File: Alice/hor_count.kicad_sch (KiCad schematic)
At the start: 270 parts, among them Q1 PASS, Q159 NOT_OC, Q160 NOT_OC, Q161 NOT_OC, Q162 NOT_OC, Q163 NOT_OC, Q164 NOT_OC, Q165 NOT_OC, Q166 NOT_OC, Q167 NOT_OC, Q168 NOT_OC, Q169 NOT_OC, Q170 NOT_OC, Q171 NOT_OC, Q172 NOT_OC, Q173 NOT_OC, Q174 NOT_OC, Q175 NOT_OC, Q176 NOT_OC, Q177 NOT_OC, Q178 NOT_OC, Q179 NOT_OC, Q180 NOT_OC, Q181 NOT_OC, Q182 NOT_OC, Q183 NOT_OC, Q184 NOT_OC, Q185 NOT_OC, Q186 NOT_OC, Q187 NOT_OC, Q188 NOT_OC, Q189 NOT_OC, Q190 NOT_OC, Q191 NOT_OC, Q192 NOT_OC, Q193 NOT_OC, Q194 NOT_OC, Q195 NOT_OC, Q196 NOT_OC, Q197 NOT_OC, Q198 NOT_OC, Q199 NOT_OC, Q2 PASS, Q200 NOT_OC, Q201 NOT_OC, Q202 NOT_OC, Q203 NOT_OC, Q204 NOT_OC, Q205 NOT_OC, Q206 NOT_OC, Q207 NOT_OC, Q208 NOT_OC, Q209 NOT_OC, Q210 NOT_OC, Q211 NOT_OC, Q212 NOT_OC, Q213 NOT_OC, Q214 NOT_OC, Q215 NOT_OC, Q216 NOT_OC, Q217 NOT_OC, Q218 NOT_OC, Q219 NOT_OC, Q220 NOT_OC, Q221 NOT_OC, Q222 NOT_OC, Q223 NOT_OC, Q224 NOT_OC, Q225 NOT_OC, Q226 NOT_OC, Q227 NOT_OC, Q228 NOT_OC, Q229 NOT_OC, Q230 NOT_OC, Q231 NOT_OC, Q232 NOT_OC, Q233 NOT_OC, Q234 NOT_OC, Q235 NOT_OC, Q236 NOT_OC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

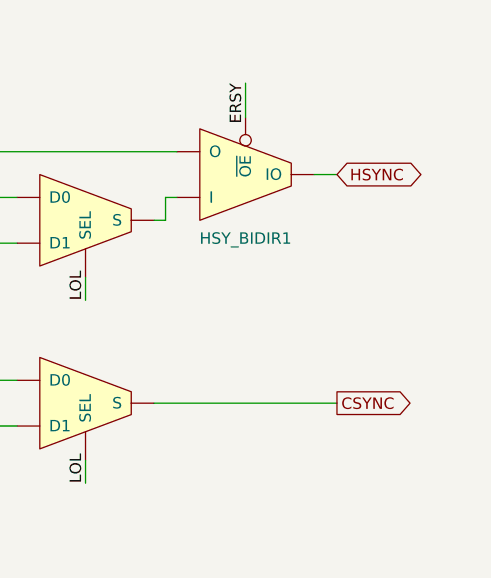
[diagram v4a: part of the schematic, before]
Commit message: RGA bus added (WIP), I/Os renamed with PAD_ prefix
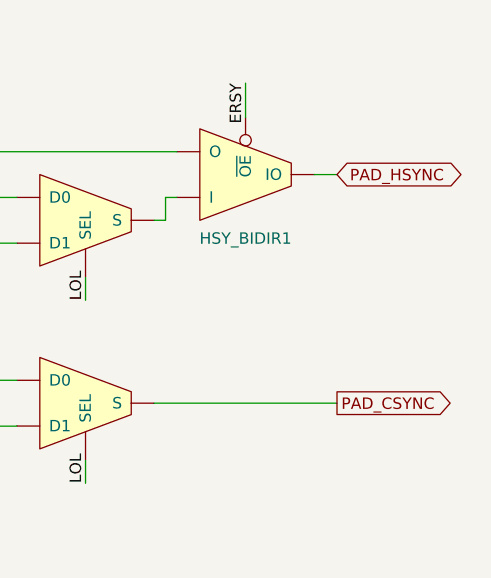
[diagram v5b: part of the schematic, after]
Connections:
- net CSYNC renamed PAD_CSYNC
- net HSYNC renamed PAD_HSYNC
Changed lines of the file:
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@@
     )
   )
-  (global_label "CSYNC" (shape output) (at 464.82 248.92 0) (fields_autoplaced)
+  (global_label "PAD_CSYNC" (shape output) (at 464.82 248.92 0) (fields_autoplaced)
     (effects (font (size 1.27 1.27)) (justify left))
-    (property "Intersheet References" "${INTERSHEET_REFS}" (id 0) (at 473.4017 248.8406 0)
+    (property "Intersheet References" "${INTERSHEET_REFS}" (id 0) (at 477.9979 248.8406 0)
       (effects (font (size 1.27 1.27)) (justify left) hide)
     )
@@
     )
   )
-  (global_label "HSYNC" (shape bidirectional) (at 464.82 223.52 0) (fields_autoplaced)
+  (global_label "PAD_HSYNC" (shape bidirectional) (at 464.82 223.52 0) (fields_autoplaced)
     (effects (font (size 1.27 1.27)) (justify left))
-    (property "Intersheet References" "${INTERSHEET_REFS}" (id 0) (at 473.4621 223.4406 0)
+    (property "Intersheet References" "${INTERSHEET_REFS}" (id 0) (at 478.0583 223.4406 0)
       (effects (font (size 1.27 1.27)) (justify left) hide)
     )

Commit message: Some refactoring : BEAMCON0 and BPLCON0 moved to the top sheet, CLOCKGEN added
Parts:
- removed BEAMCON0_LB0, BEAMCON0_LB10, BEAMCON0_LB11, BEAMCON0_LB2, BEAMCON0_LB3, BEAMCON0_LB4, BEAMCON0_LB8: LB2, symbol NMOS:LB2
- removed NOT_11: NOT, symbol NMOS:NOT
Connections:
- net RESET: now also OR_7.2; no longer OR_7.3
- net RHSH: now also OR_7.3; no longer OR_7.2
- no-connect marks 8 -> 1
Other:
- moved on the sheet: HEND_FF1, HSY_BIDIR1, VARHSY_SR1

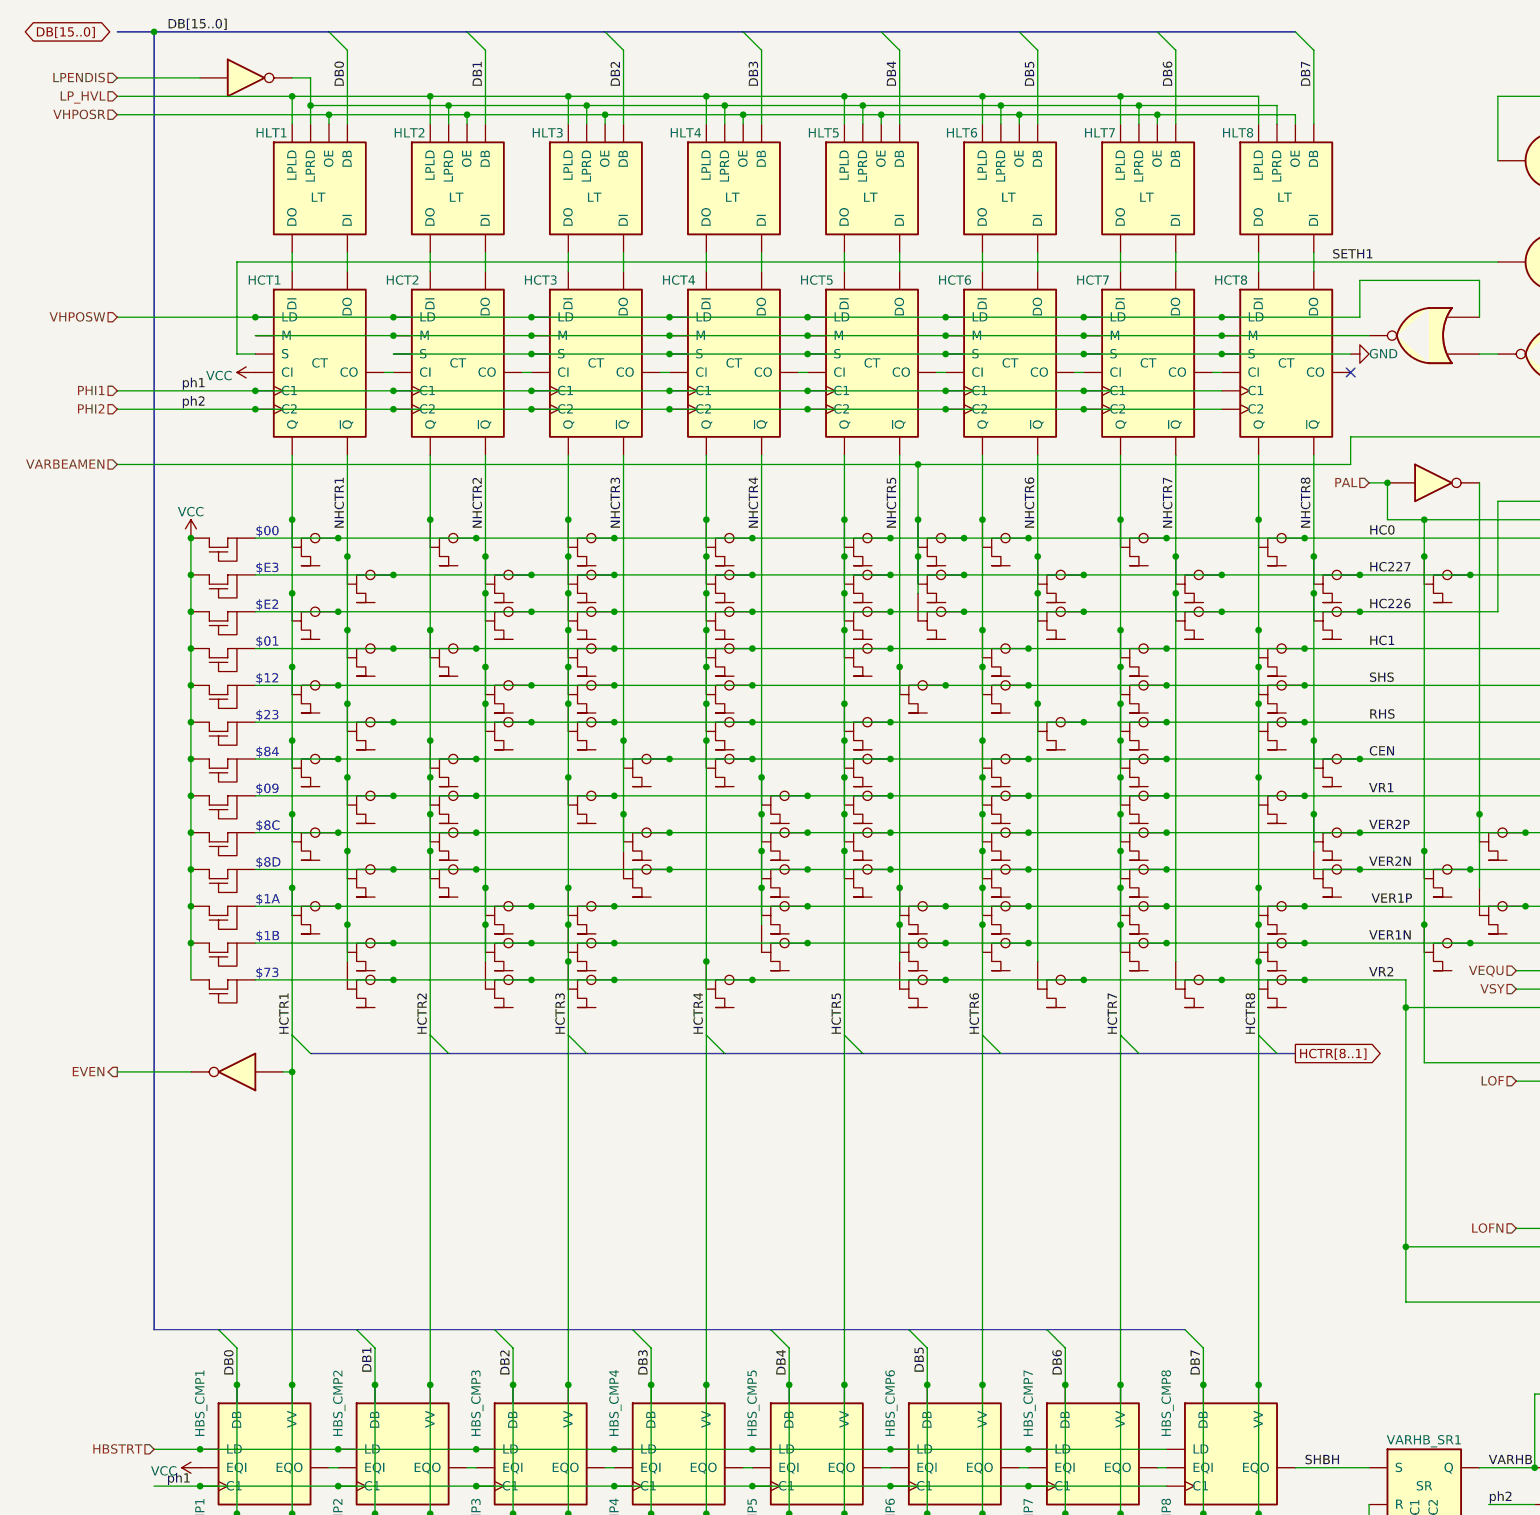
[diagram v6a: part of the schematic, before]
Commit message: Plane DMA sheet added
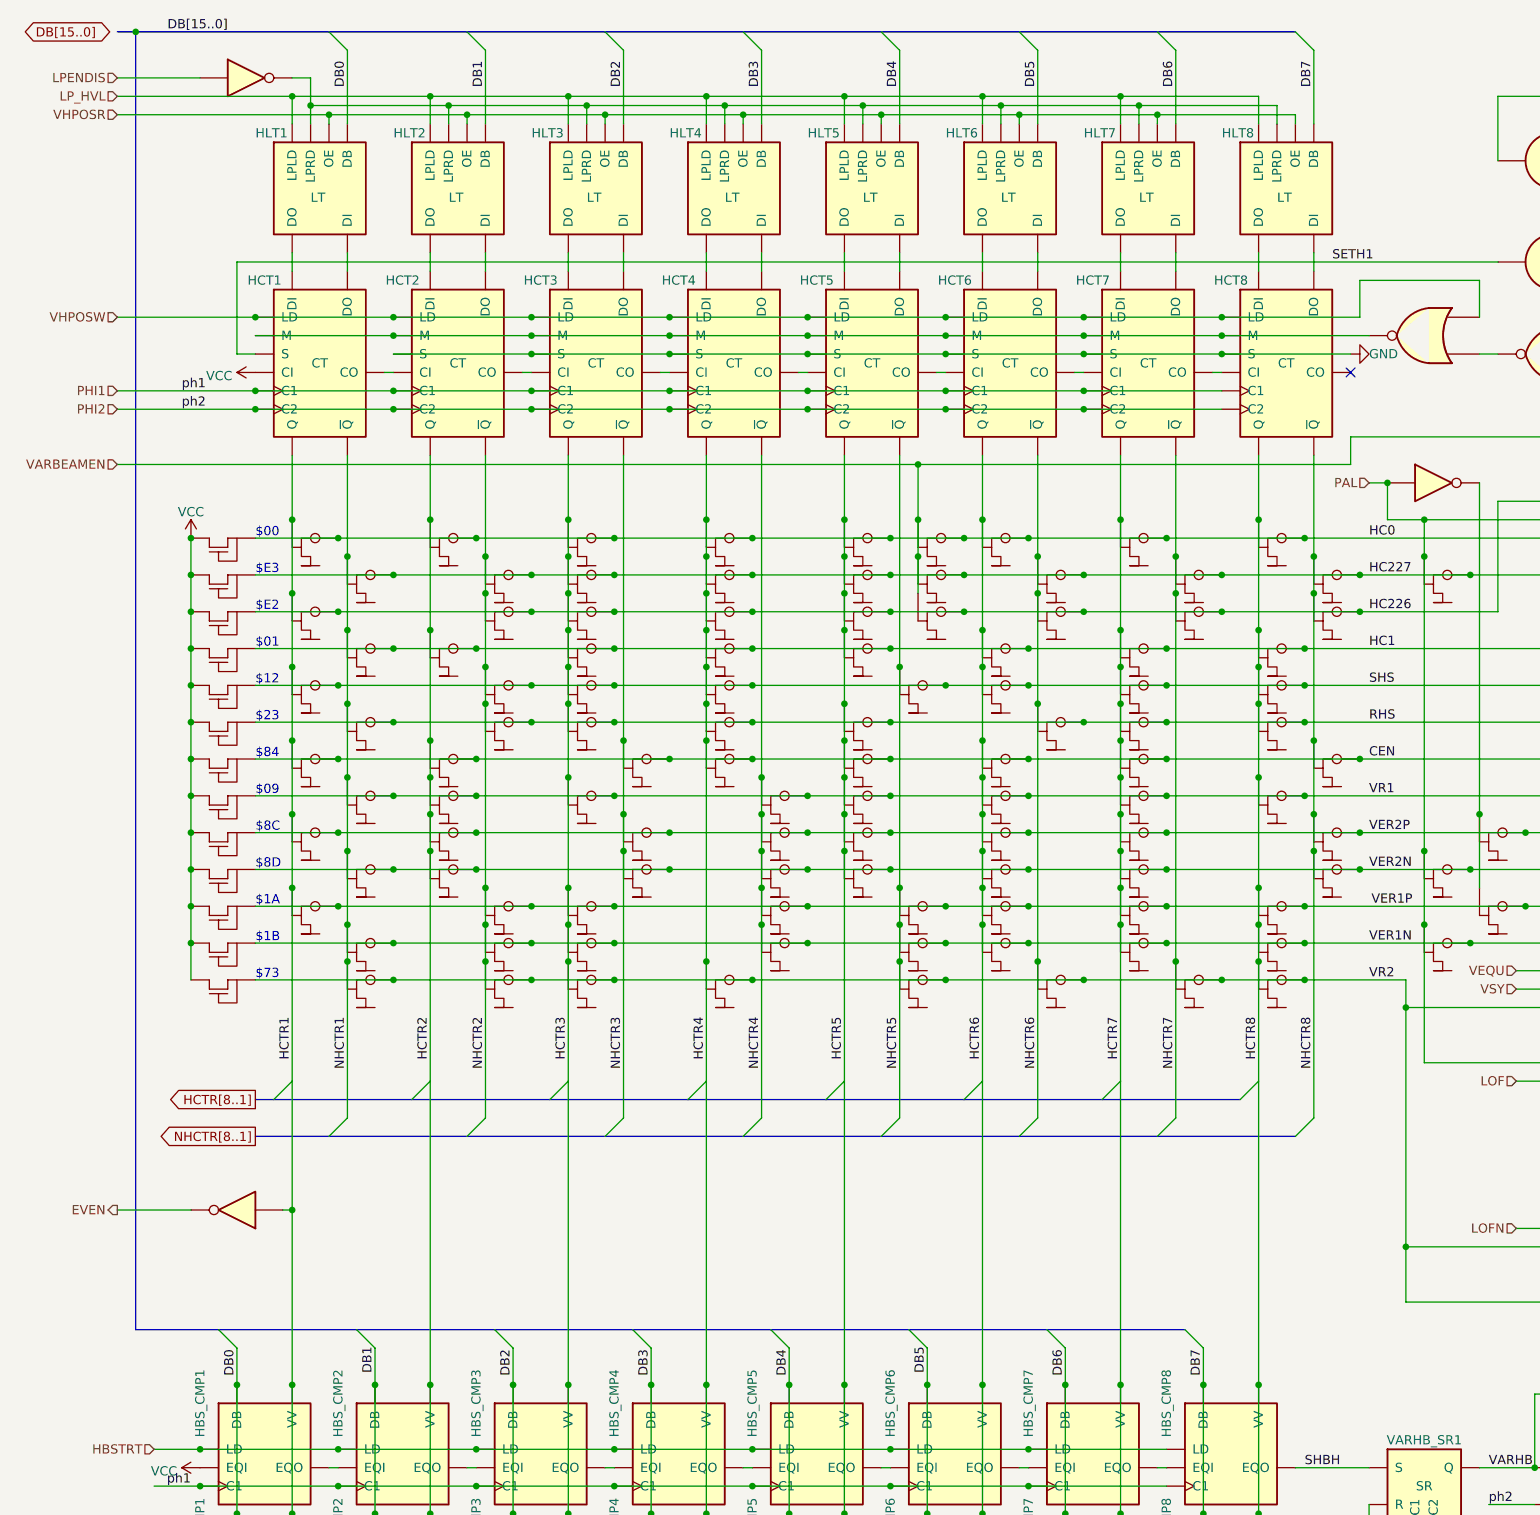
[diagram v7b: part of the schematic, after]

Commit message: Schematics have been annotated
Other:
- note added: "ECS/AGA Horizontal Comparators"
- note added: "Fixed Horizontal Comparators"
- note added: "Genlock logic"
- note added: "Half-cycle delay for Long Lines"
- note added: "Horizontal Counter with Light Pen latches"
- note added: "Long Line flip-flop"
- note added: "Synchro / Blanking logic"
- moved on the sheet: CSY_SR1, HBC_CMP1, HBC_CMP2, HBC_CMP3, HBC_CMP4, HBC_CMP5, HBC_CMP6, HBC_CMP7, HBC_CMP8, HBS_CMP1, HBS_CMP2, HBS_CMP3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
